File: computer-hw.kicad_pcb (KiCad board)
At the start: 2 copper layers, 156 x 143.9 mm, 95 parts, among them J1 Conn_01x08, J2 Barrel_Jack, J3 Conn_01x04, J4 Conn_01x04, J5 Conn_01x16, J6 Conn_01x08, SW1 SW_Push, SW2 B_UP, SW3 B_DOWN, SW4 B_LEFT, SW5 B_RIGHT, SW6 B_BACK, SW7 B_OK, U1 2 MHz, U10 2716, U11 74LS04, U12 4028, U13 74LS04, U14 KR537RU2, U15 KR537RU2, U16 KR537RU2, U17 KR537RU2, U18 KR537RU2, U19 KR537RU2, U2 AP1117-33, U20 KR537RU2, U21 KR537RU2, U22 8255, U23 CF, U24 SN74LVC8T245, U25 SN74LVC8T245, U26 DISPLAY_MOD, U27 KR580VV51A, U28 1.8432 MHz, U3 Z80CPU, U4 74HC245, U5 74HC245, U6 74HC245, U7 2716, U8 2716, U9 2716

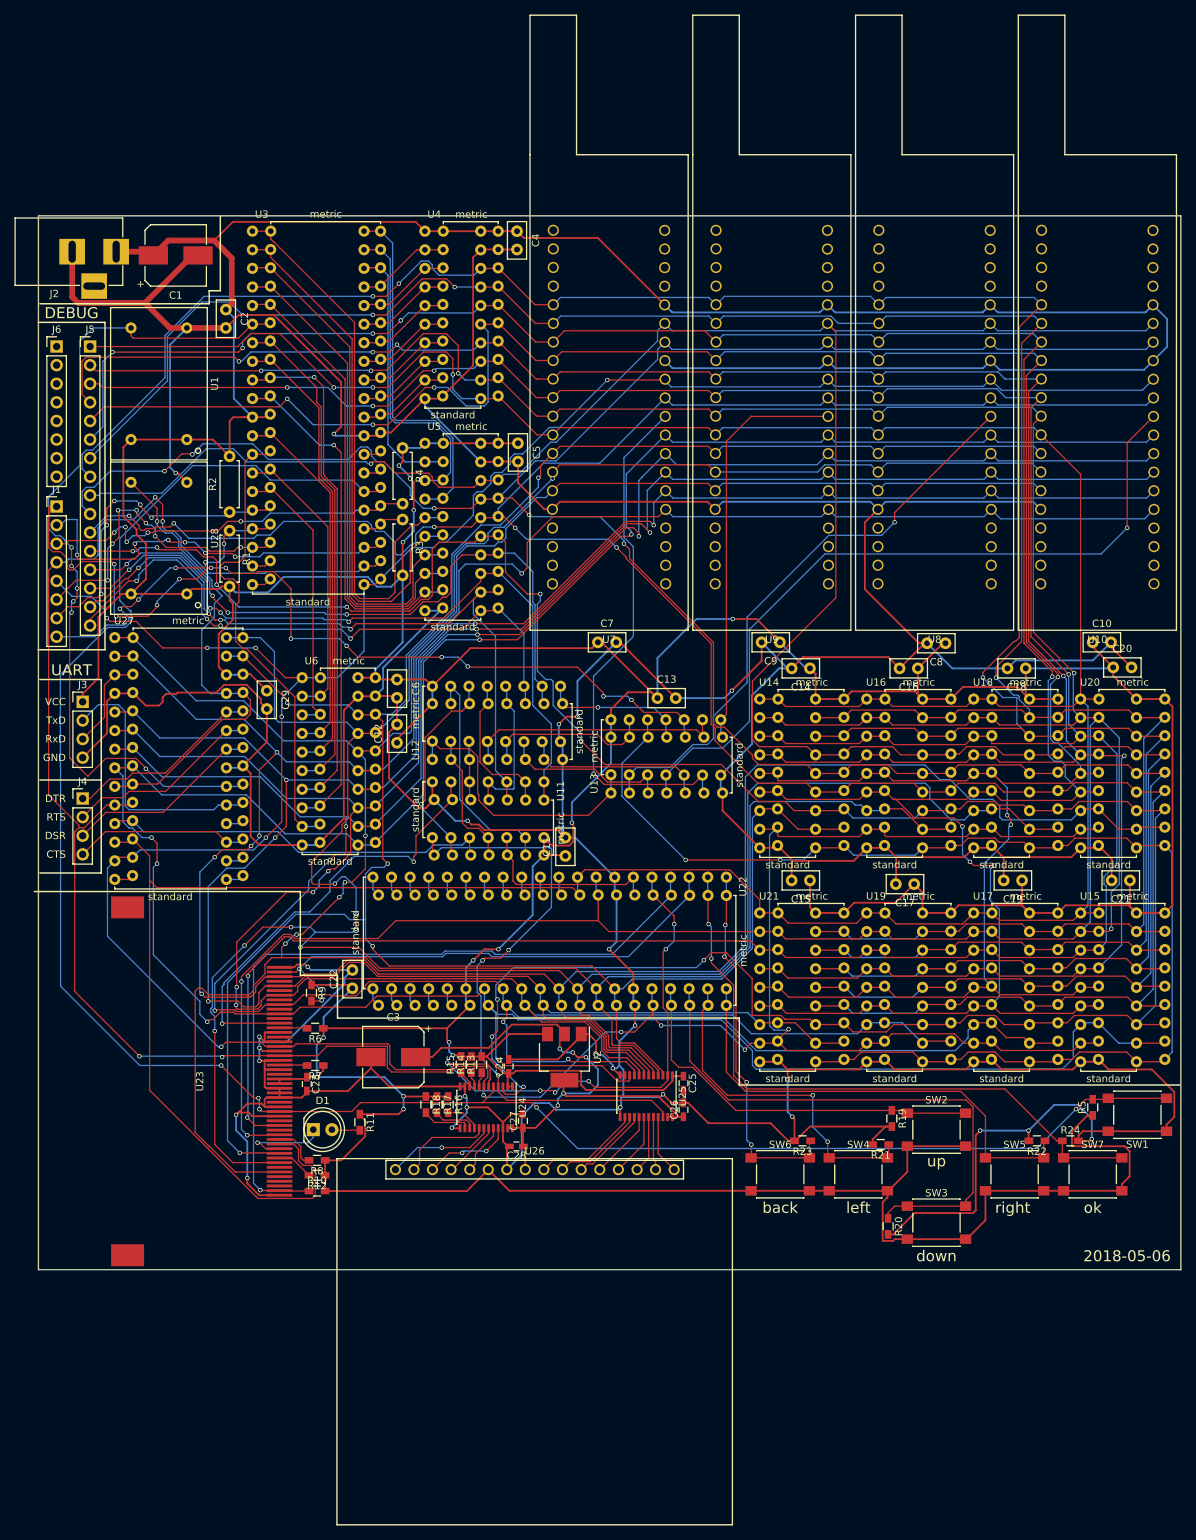
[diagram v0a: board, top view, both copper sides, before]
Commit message: add fixes so that the pcb actually meets the design rules
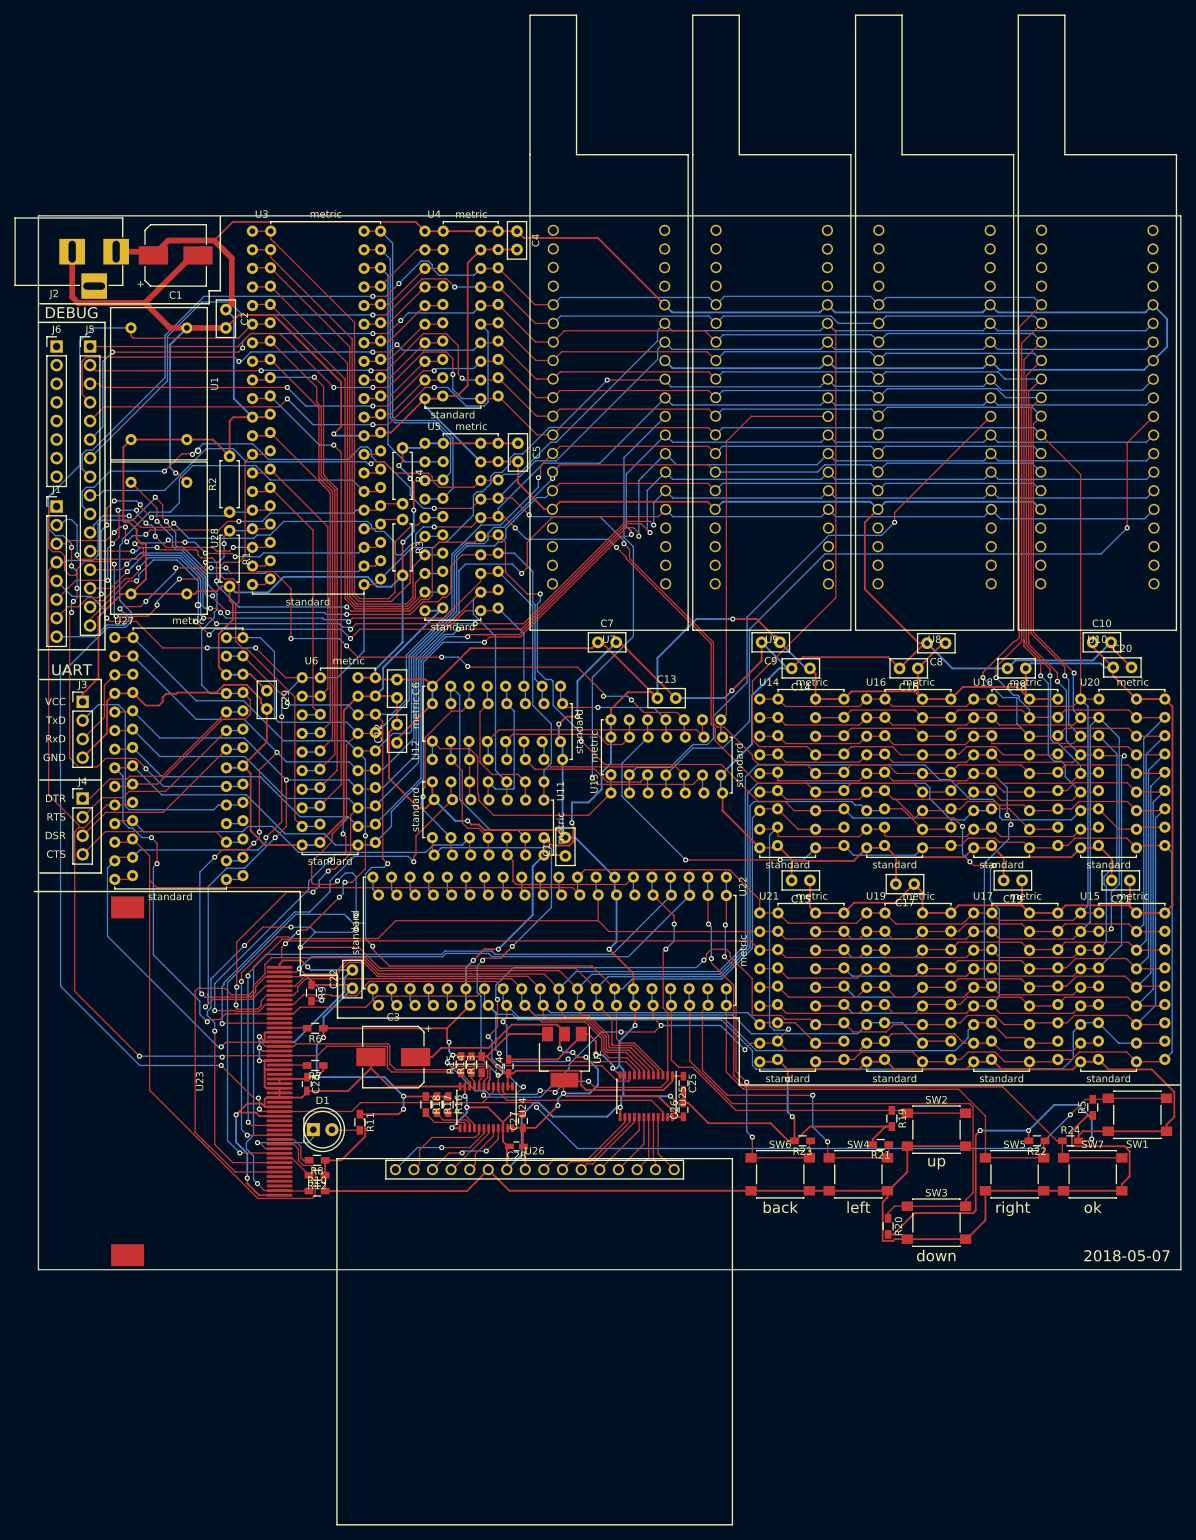
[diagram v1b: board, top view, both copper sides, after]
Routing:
- net GND: track 1040.5 -> 1043.1 mm
- net VCC: track 1068.5 -> 1071.0 mm
- net /D6: track 372.6 -> 374.8 mm
- net A15: track 83.3 -> 85.3 mm
- net /D2: track 399.1 -> 400.9 mm
- net /D1: track 375.7 -> 377.4 mm
- net A13: track 101.3 -> 103.0 mm
- net /RESET: track 276.4 -> 278.0 mm
- net /Decoding//DISPLAY_EN: track 83.1 -> 84.7 mm
- net /A11: track 346.6 -> 348.1 mm
- net /EXP_EN: track 121.7 -> 123.0 mm
- net /D4: track 328.1 -> 329.2 mm
- net A14: track 97.6 -> 98.7 mm
- net /WR: track 378.5 -> 379.3 mm
- net Net-(J1-Pad2): track 54.3 -> 55.2 mm
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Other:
- net class Default: via_dia 0.6 -> 0.7; via_drill 0.4 -> 0.38
- net class High power: via_dia 0.6 -> 0.7; via_drill 0.4 -> 0.38
- net class Power: via_dia 0.6 -> 0.7; via_drill 0.4 -> 0.38
- rule via_min_drill: 0.3 -> 0.38
- rule via_min_size: 0.4 -> 0.7
- board text added: "2018-05-07"
- board text removed: "2018-05-06"
